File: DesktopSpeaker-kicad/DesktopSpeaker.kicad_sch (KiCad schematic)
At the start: 12 parts, among them J1 USB_C_Receptacle_USB2.0_16P, J2 HEAD_OUT, J3 AUX_IN, U1 BM83SM1-00TA, U10 TPA6132A2RTER, U2 PCM2902CDBR, U3 STM32G031K8T6, U6 TAS5825MRHBR, U7 TAS5825MRHBR, U8 TS5A23157DGSR, U9 TS5A23157DGSR

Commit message: Integrate TPS25730D PD and BQ25792 charger into active project (5-20 V); update BOM, plan, handover, preview
Co-Authored-By: Claude Sonnet 5.5 <noreply@anthropic.com>
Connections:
- no-connect marks 2 -> 7
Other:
- sheet Battery_Charger ports: added CHG_SYS_ENABLE; removed none
- sheet USB_PD ports: added PDCTRL_SCL, PDCTRL_SDA, PD_PLUG_EVENT, PD_SINK_EN; removed GND
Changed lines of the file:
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@@
 (no_connect (at 49.53 239.86))
 (no_connect (at 49.53 255.1))
-(sheet (at 100.33 139.7) (size 45.72 48.26) (stroke (width 0) (type default)) (fill (color 255 255 255 0)) (property "Sheet name" "USB_PD" (at 100.33 138.42999999999998 0) (effects (font (size 1.27 1.27)) (justify left))) (property "Sheet file" "USB_PD.kicad_sch" (at 100.33 187.95999999999998 0) (effects (font (size 1.27 1.27)) (hide yes))) (pin "USB_VBUS" input (at 100.33 147.32 180) (effects (font (size 1 1)) (justify left bottom))) (pin "USB_CC1" input (at 100.33 154.94 180) (effects (font (size 1 1)) (justify left bottom))) (pin "USB_CC2" input (at 100.33 162.56 180) (effects (font (size 1 1)) (justify left bottom))) (pin "GND" input (at 100.33 170.18 180) (effects (font (size 1 1)) (justify left bottom))) (pin "VBUS_PD" output (at 146.05 147.32 0) (effects (font (size 1 1)) (justify right bottom))) (instances (project "DesktopSpeaker" (path "/feda53ed-537d-4f88-9436-c6075776255b" (page "2")))) (pin "USB_AUX_5V" output (at 146.05 144.78 0) (effects (font (size 1 1)) (justify right bottom))))
-(sheet (at 166.37 139.7) (size 53.34 66.04) (stroke (width 0) (type default)) (fill (color 255 255 255 0)) (property "Sheet name" "Battery_Charger" (at 166.37 138.42999999999998 0) (effects (font (size 1.27 1.27)) (justify left))) (property "Sheet file" "Battery_Charger.kicad_sch" (at 166.37 205.74 0) (effects (font (size 1.27 1.27)) (hide yes))) (pin "VBUS_PD" input (at 166.37 147.32 180) (effects (font (size 1 1)) (justify left bottom))) (pin "CHG_ENABLE" input (at 166.37 165.1 180) (effects (font (size 1 1)) (justify left bottom))) (pin "CHG_VIO_3V0" input (at 166.37 195.58 180) (effects (font (size 1 1)) (justify left bottom))) (pin "SYS_RAW" output (at 219.71 147.32 0) (effects (font (size 1 1)) (justify right bottom))) (pin "BAT_PACK" bidirectional (at 219.71 157.48 0) (effects (font (size 1 1)) (justify right bottom))) (pin "CHG_SCL" bidirectional (at 219.71 170.18 0) (effects (font (size 1 1)) (justify right bottom))) (pin "CHG_SDA" bidirectional (at 219.71 180.34 0) (effects (font (size 1 1)) (justify right bottom))) (pin "CHG_INT" output (at 219.71 195.58 0) (effects (font (size 1 1)) (justify right bottom))) (instances (project "DesktopSpeaker" (path "/feda53ed-537d-4f88-9436-c6075776255b" (page "3")))))
+(sheet (at 100.33 139.7) (size 45.72 48.26) (stroke (width 0) (type default)) (fill (color 255 255 255 0)) (property "Sheet name" "USB_PD" (at 100.33 138.42999999999998 0) (effects (font (size 1.27 1.27)) (justify left))) (property "Sheet file" "USB_PD.kicad_sch" (at 100.33 187.95999999999998 0) (effects (font (size 1.27 1.27)) (hide yes))) (pin "USB_VBUS" input (at 100.33 147.32 180) (effects (font (size 1 1)) (justify left bottom))) (pin "USB_CC1" input (at 100.33 154.94 180) (effects (font (size 1 1)) (justify left bottom))) (pin "USB_CC2" input (at 100.33 162.56 180) (effects (font (size 1 1)) (justify left bottom))) (pin "VBUS_PD" output (at 146.05 147.32 0) (effects (font (size 1 1)) (justify right bottom))) (instances (project "DesktopSpeaker" (path "/feda53ed-537d-4f88-9436-c6075776255b" (page "2")))) (pin "PD_PLUG_EVENT" output (at 146.05 154.94 0) (effects (font (size 1 1)) (justify right bottom))) (pin "PD_SINK_EN" output (at 146.05 162.56 0) (effects (font (size 1 1)) (justify right bottom))) (pin "PDCTRL_SCL" bidirectional (at 146.05 170.18 0) (effects (font (size 1 1)) (justify right bottom))) (pin "PDCTRL_SDA" bidirectional (at 146.05 177.8 0) (effects (font (size 1 1)) (justify right bottom))) (pin "USB_AUX_5V" output (at 146.05 144.78 0) (effects (font (size 1 1)) (justify right bottom))))
+(sheet (at 166.37 139.7) (size 53.34 66.04) (stroke (width 0) (type default)) (fill (color 255 255 255 0)) (property "Sheet name" "Battery_Charger" (at 166.37 138.42999999999998 0) (effects (font (size 1.27 1.27)) (justify left))) (property "Sheet file" "Battery_Charger.kicad_sch" (at 166.37 205.74 0) (effects (font (size 1.27 1.27)) (hide yes))) (pin "VBUS_PD" input (at 166.37 147.32 180) (effects (font (size 1 1)) (justify left bottom))) (pin "CHG_ENABLE" input (at 166.37 165.1 180) (effects (font (size 1 1)) (justify left bottom))) (pin "CHG_VIO_3V0" input (at 166.37 195.58 180) (effects (font (size 1 1)) (justify left bottom))) (pin "CHG_SYS_ENABLE" input (at 166.37 175.26 180) (effects (font (size 1 1)) (justify left bottom))) (pin "SYS_RAW" output (at 219.71 147.32 0) (effects (font (size 1 1)) (justify right bottom))) (pin "BAT_PACK" bidirectional (at 219.71 157.48 0) (effects (font (size 1 1)) (justify right bottom))) (pin "CHG_SCL" bidirectional (at 219.71 170.18 0) (effects (font (size 1 1)) (justify right bottom))) (pin "CHG_SDA" bidirectional (at 219.71 180.34 0) (effects (font (size 1 1)) (justify right bottom))) (pin "CHG_INT" output (at 219.71 195.58 0) (effects (font (size 1 1)) (justify right bottom))) (instances (project "DesktopSpeaker" (path "/feda53ed-537d-4f88-9436-c6075776255b" (page "3")))))
 (sheet (at 240.03 139.7) (size 50.8 66.04) (stroke (width 0) (type default)) (fill (color 255 255 255 0)) (property "Sheet name" "Fuel_Gauge_Power" (at 240.03 138.42999999999998 0) (effects (font (size 1.27 1.27)) (justify left))) (property "Sheet file" "Fuel_Gauge_Power.kicad_sch" (at 240.03 205.74 0) (effects (font (size 1.27 1.27)) (hide yes))) (pin "SYS_RAW" input (at 240.03 147.32 180) (effects (font (size 1 1)) (justify left bottom))) (pin "BAT_PACK" input (at 240.03 157.48 180) (effects (font (size 1 1)) (justify left bottom))) (pin "GAUGE_SCL" input (at 240.03 170.18 180) (effects (font (size 1 1)) (justify left bottom))) (pin "GAUGE_SDA" bidirectional (at 240.03 180.34 180) (effects (font (size 1 1)) (justify left bottom))) (pin "3V_AO" output (at 290.83 147.32 0) (effects (font (size 1 1)) (justify right bottom))) (pin "GAUGE_ALRT_N" output (at 290.83 195.58 0) (effects (font (size 1 1)) (justify right bottom))) (instances (project "DesktopSpeaker" (path "/feda53ed-537d-4f88-9436-c6075776255b" (page "4")))) (pin "USB_AUX_5V" input (at 240.03 144.78 180) (effects (font (size 1 1)) (justify left bottom))))
 (wire (pts (xy 146.05 147.32) (xy 166.37 147.32)) (stroke (width 0) (type default)))
@@
 (wire (pts (xy 290.83 195.58) (xy 295.91 195.58)) (stroke (width 0) (type default)))
 (label "GAUGE_ALRT_N" (at 295.91 195.58 0) (effects (font (size 1 1)) (justify left bottom)))
-(wire (pts (xy 100.33 170.18) (xy 95.25 170.18)) (stroke (width 0) (type default)))
-(wire (pts (xy 95.25 170.18) (xy 95.25 175.26)) (stroke (width 0) (type default)))
-(symbol (lib_id "power:GND") (at 95.25 175.26 0) (unit 1) (in_bom no) (on_board no) (property "Reference" "#PWR301" (at 95.25 179.07 0) (effects (font (size 1.27 1.27)) (hide yes))) (property "Value" "GND" (at 95.25 180.34 0) (effects (font (size 1.27 1.27)))) (pin "1") (instances (project "DesktopSpeaker" (path "/feda53ed-537d-4f88-9436-c6075776255b" (reference "#PWR301") (unit 1)))))
 (sheet (at 166.37 224.79) (size 53.34 43.18) (stroke (width 0) (type default)) (fill (color 255 255 255 0)) (property "Sheet name" "Bluetooth_Power" (at 166.37 223.51999999999998 0) (effects (font (size 1.27 1.27)) (justify left))) (property "Sheet file" "Bluetooth_Power.kicad_sch" (at 166.37 267.96999999999997 0) (effects (font (size 1.27 1.27)) (hide yes))) (pin "SYS_RAW" input (at 166.37 232.41 180) (effects (font (size 1 1)) (justify left bottom))) (pin "BT_PWR_EN" input (at 166.37 243.84 180) (effects (font (size 1 1)) (justify left bottom))) (pin "BT_FORCE_PWM" input (at 166.37 254.0 180) (effects (font (size 1 1)) (justify left bottom))) (pin "3V8_BT" output (at 219.71 259.08 0) (effects (font (size 1 1)) (justify right bottom))) (instances (project "DesktopSpeaker" (path "/feda53ed-537d-4f88-9436-c6075776255b" (page "5")))))
 (sheet (at 240.03 224.79) (size 50.8 43.18) (stroke (width 0) (type default)) (fill (color 255 255 255 0)) (property "Sheet name" "Logic_Audio_Power" (at 240.03 223.51999999999998 0) (effects (font (size 1.27 1.27)) (justify left))) (property "Sheet file" "Logic_Audio_Power.kicad_sch" (at 240.03 267.96999999999997 0) (effects (font (size 1.27 1.27)) (hide yes))) (pin "SYS_RAW" input (at 240.03 232.41 180) (effects (font (size 1 1)) (justify left bottom))) (pin "5V_LOGIC_EN" input (at 240.03 245.11 180) (effects (font (size 1 1)) (justify left bottom))) (pin "5V_LOGIC" output (at 290.83 232.41 0) (effects (font (size 1 1)) (justify right bottom))) (instances (project "DesktopSpeaker" (path "/feda53ed-537d-4f88-9436-c6075776255b" (page "6")))))
@@
 (wire (pts (xy 153.67 134.62) (xy 234.95 134.62)) (stroke (width 0) (type default)))
 (wire (pts (xy 234.95 134.62) (xy 234.95 144.78)) (stroke (width 0) (type default)))
-(wire (pts (xy 234.95 144.78) (xy 240.03 144.78)) (stroke (width 0) (type default))))
+(wire (pts (xy 234.95 144.78) (xy 240.03 144.78)) (stroke (width 0) (type default)))
+(no_connect (at 146.05 154.94))
+(no_connect (at 146.05 162.56))
+(no_connect (at 146.05 170.18))
+(no_connect (at 146.05 177.8))
+(no_connect (at 166.37 175.26))
+)

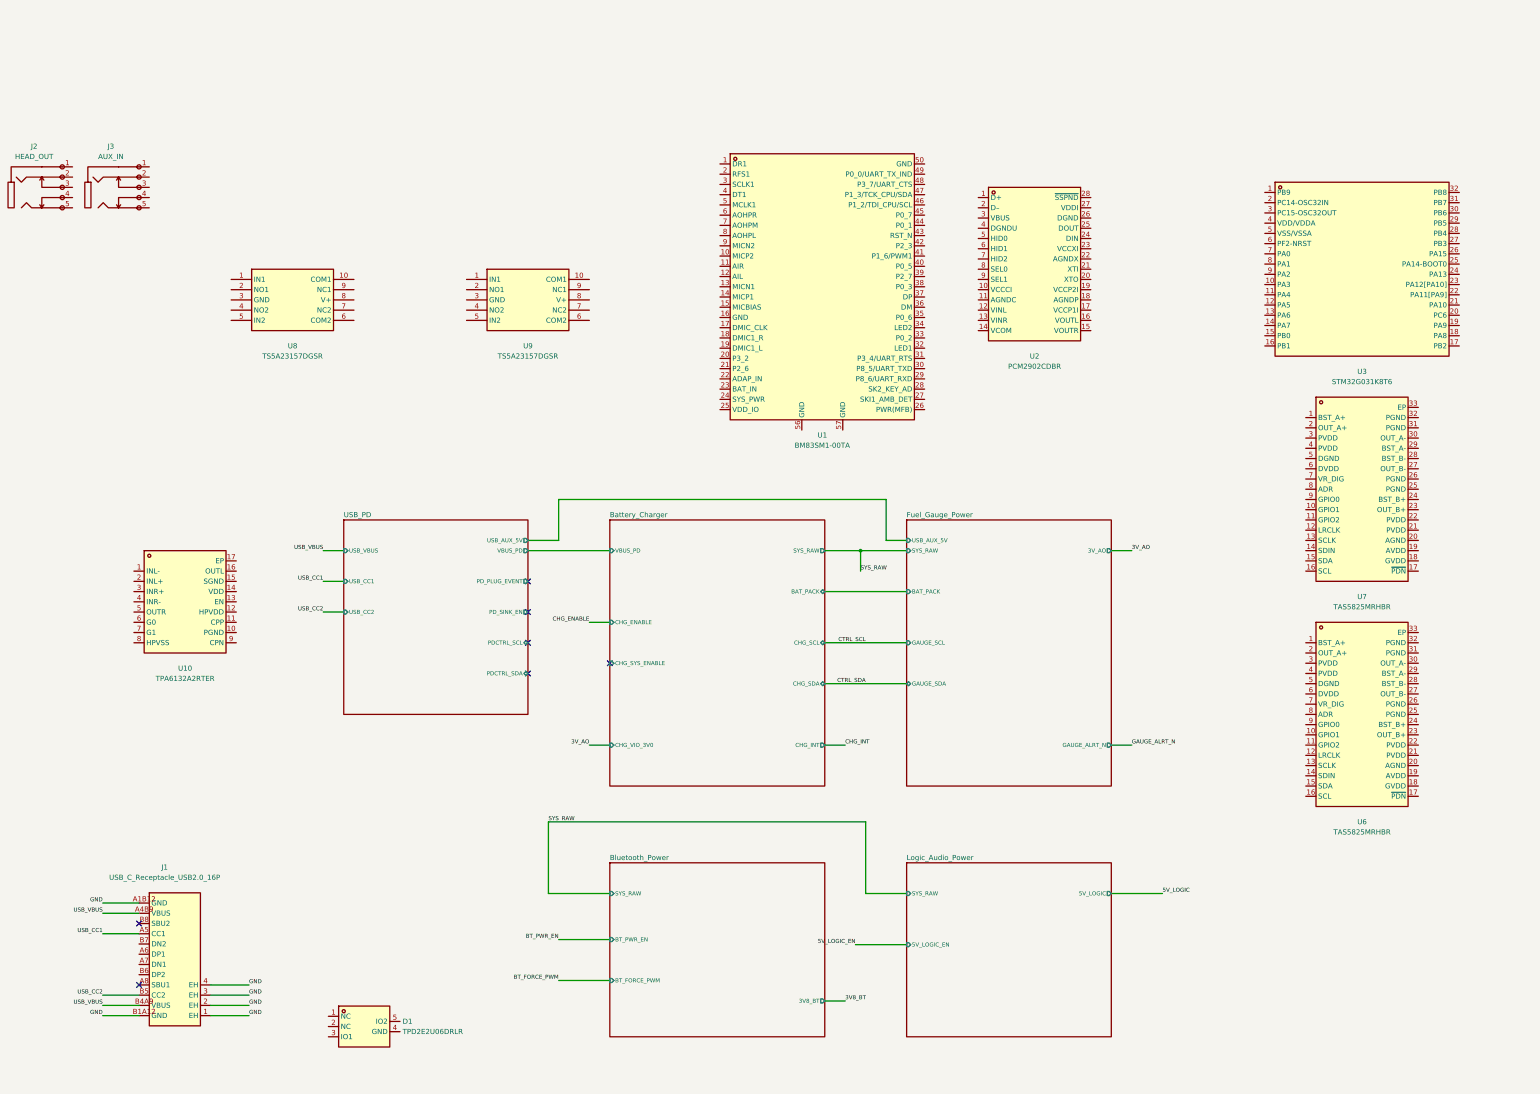
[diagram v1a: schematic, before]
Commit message: Capture MCU sheet (STM32G031) with pin allocation and power-block connections
Co-Authored-By: Claude Sonnet 5.5 <noreply@anthropic.com>
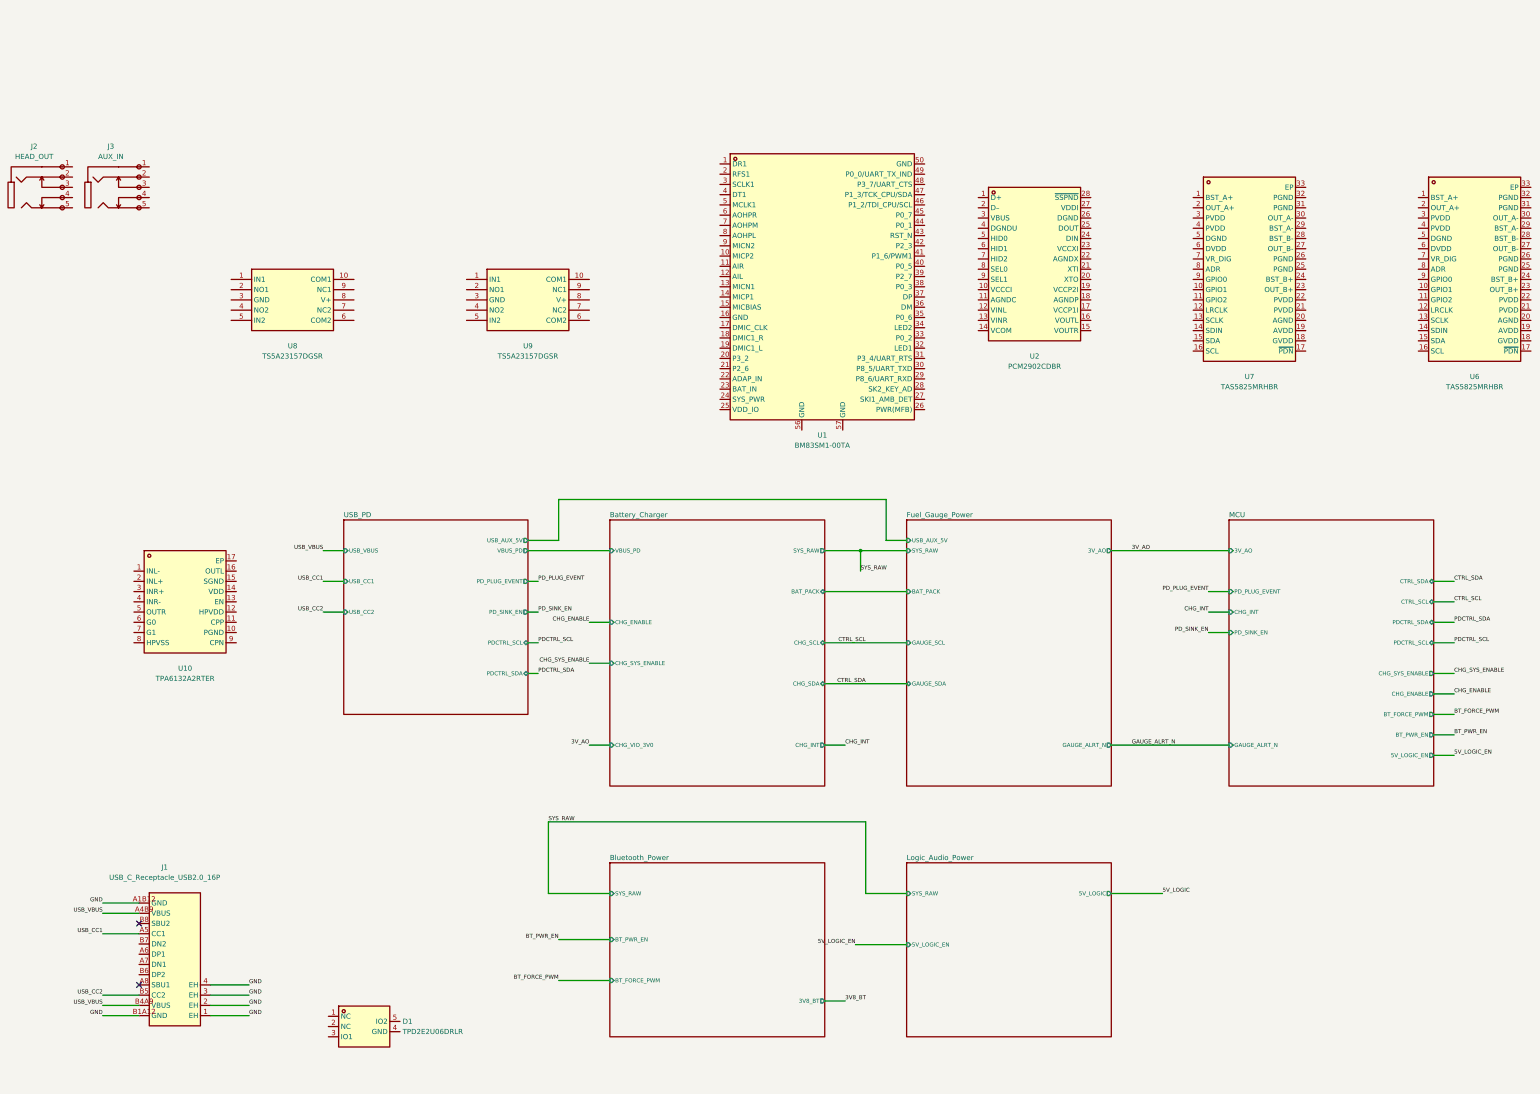
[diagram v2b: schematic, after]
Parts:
- removed U3: STM32G031K8T6, DesktopSpeaker:STM32G031K8T6, symbol STM32G031K8T6:STM32G031K8T6
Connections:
- no-connect marks 7 -> 2
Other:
- added sheet MCU (MCU.kicad_sch)
- moved on the sheet: U6, U7

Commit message: Capture USB audio (PCM2902C) child sheet, J1 data path and D1 ground
Co-Authored-By: Claude Sonnet 5.5 <noreply@anthropic.com>
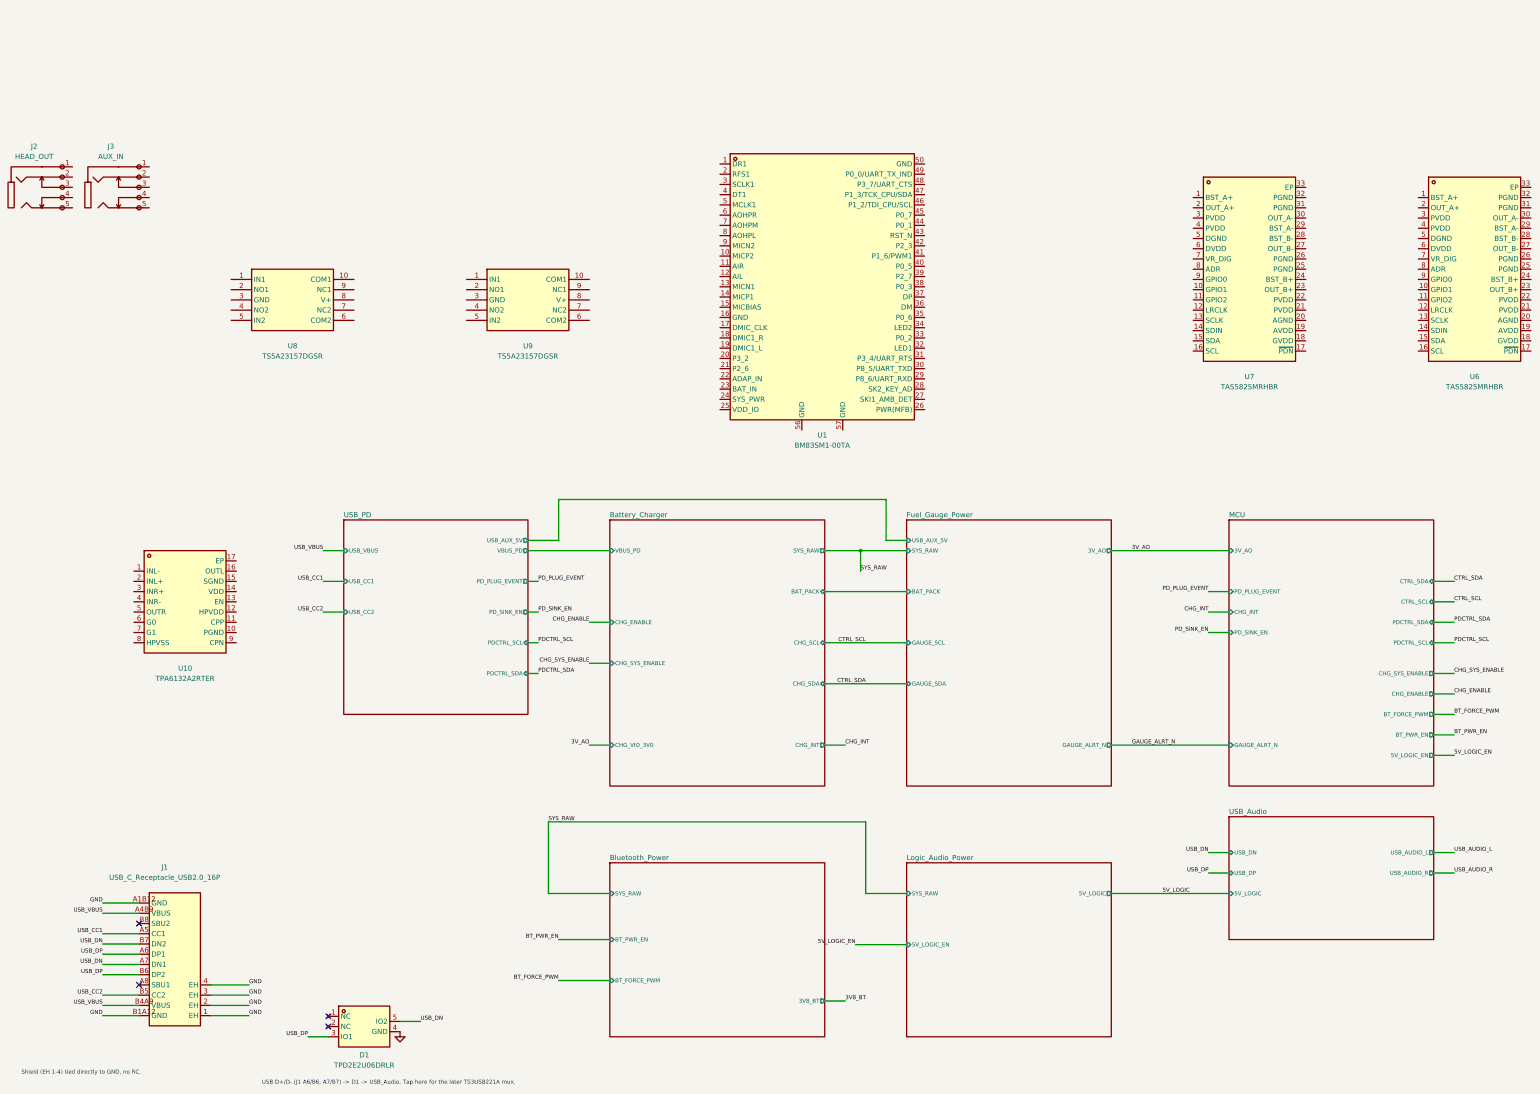
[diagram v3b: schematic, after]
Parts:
- removed U2: PCM2902CDBR, DesktopSpeaker:PCM2902CDBR, symbol PCM2902CDBR:PCM2902CDBR
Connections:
- net GND: now also D1.4 (GND)
- net USB_DP: now reaches D1.3 (IO1)
- net USB_DP: now also J1.A6 (DP1), J1.B6 (DP2)
- net USB_DN: now reaches D1.5 (IO2)
- net USB_DN: now also J1.A7 (DN1), J1.B7 (DN2)
- no-connect marks 2 -> 4
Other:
- added sheet USB_Audio (USB_Audio.kicad_sch)
- note added: "Shield (EH 1-4) tied directly to GND, no RC."
- note added: "USB D+/D- (J1 A6/B6, A7/B7) -> D1 -> USB_Audio. Tap here for the later TS3USB221A mux."
